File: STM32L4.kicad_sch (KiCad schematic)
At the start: 29 parts, among them J3 Conn_01x04_Pin, SW1 SW, U17 TCAN334, U18 STM32L476RGTx, U19 MR20H40, Y1 8 MHZ Oscillator

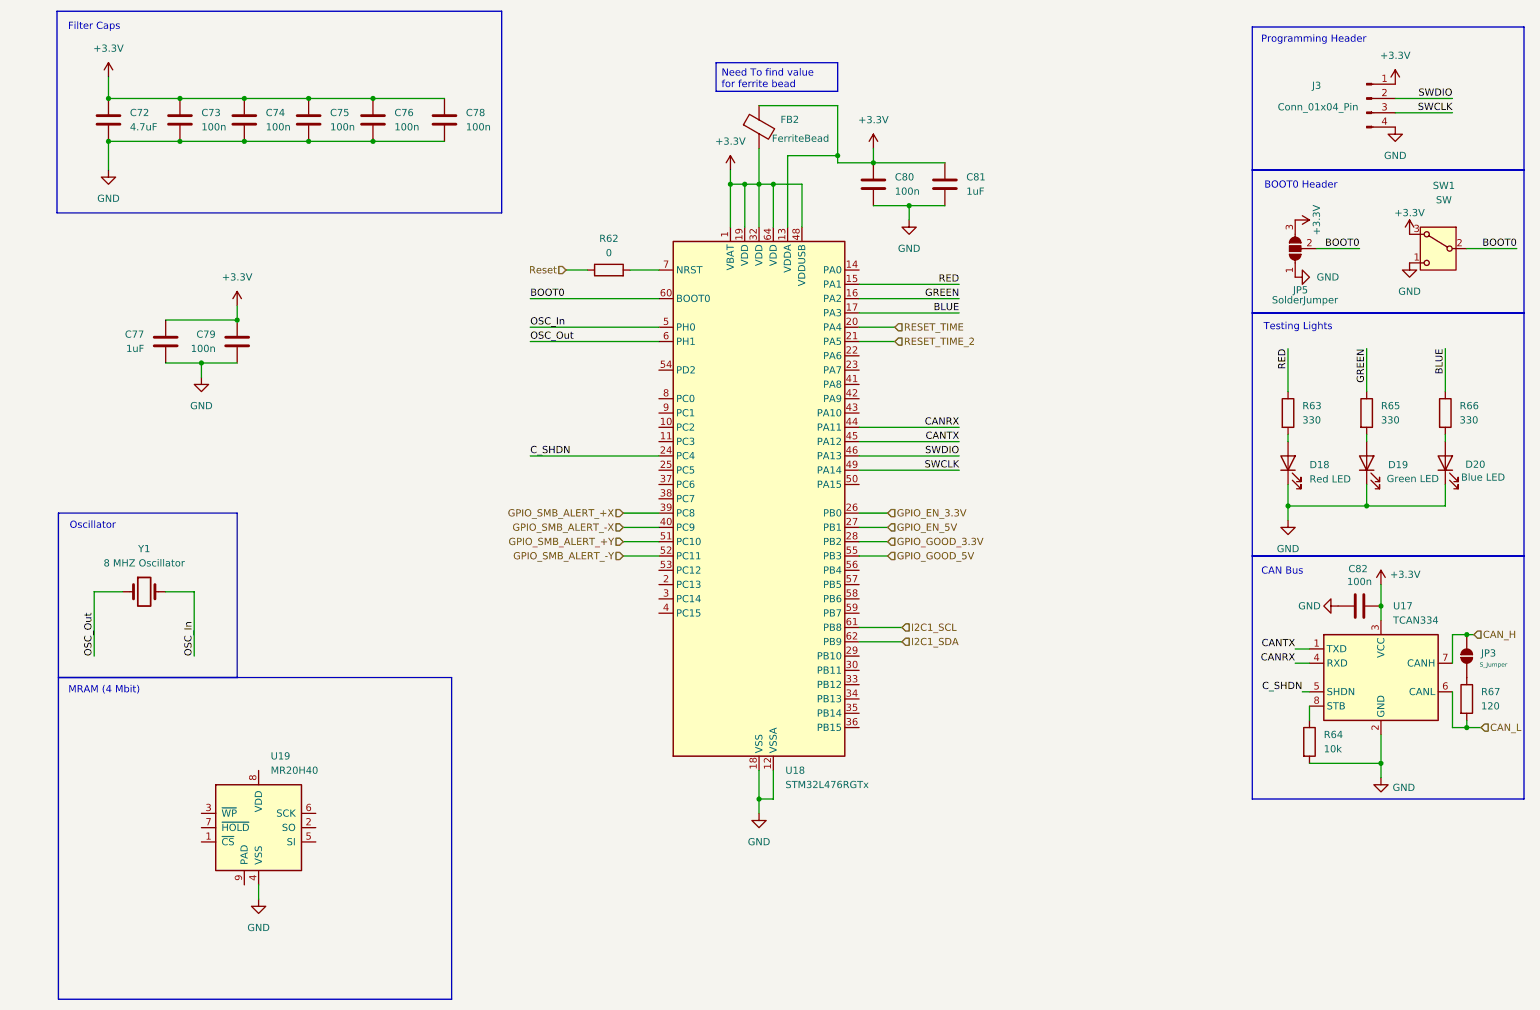
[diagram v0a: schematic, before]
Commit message: Added cap to output of lines
based on LTSpice Simulation
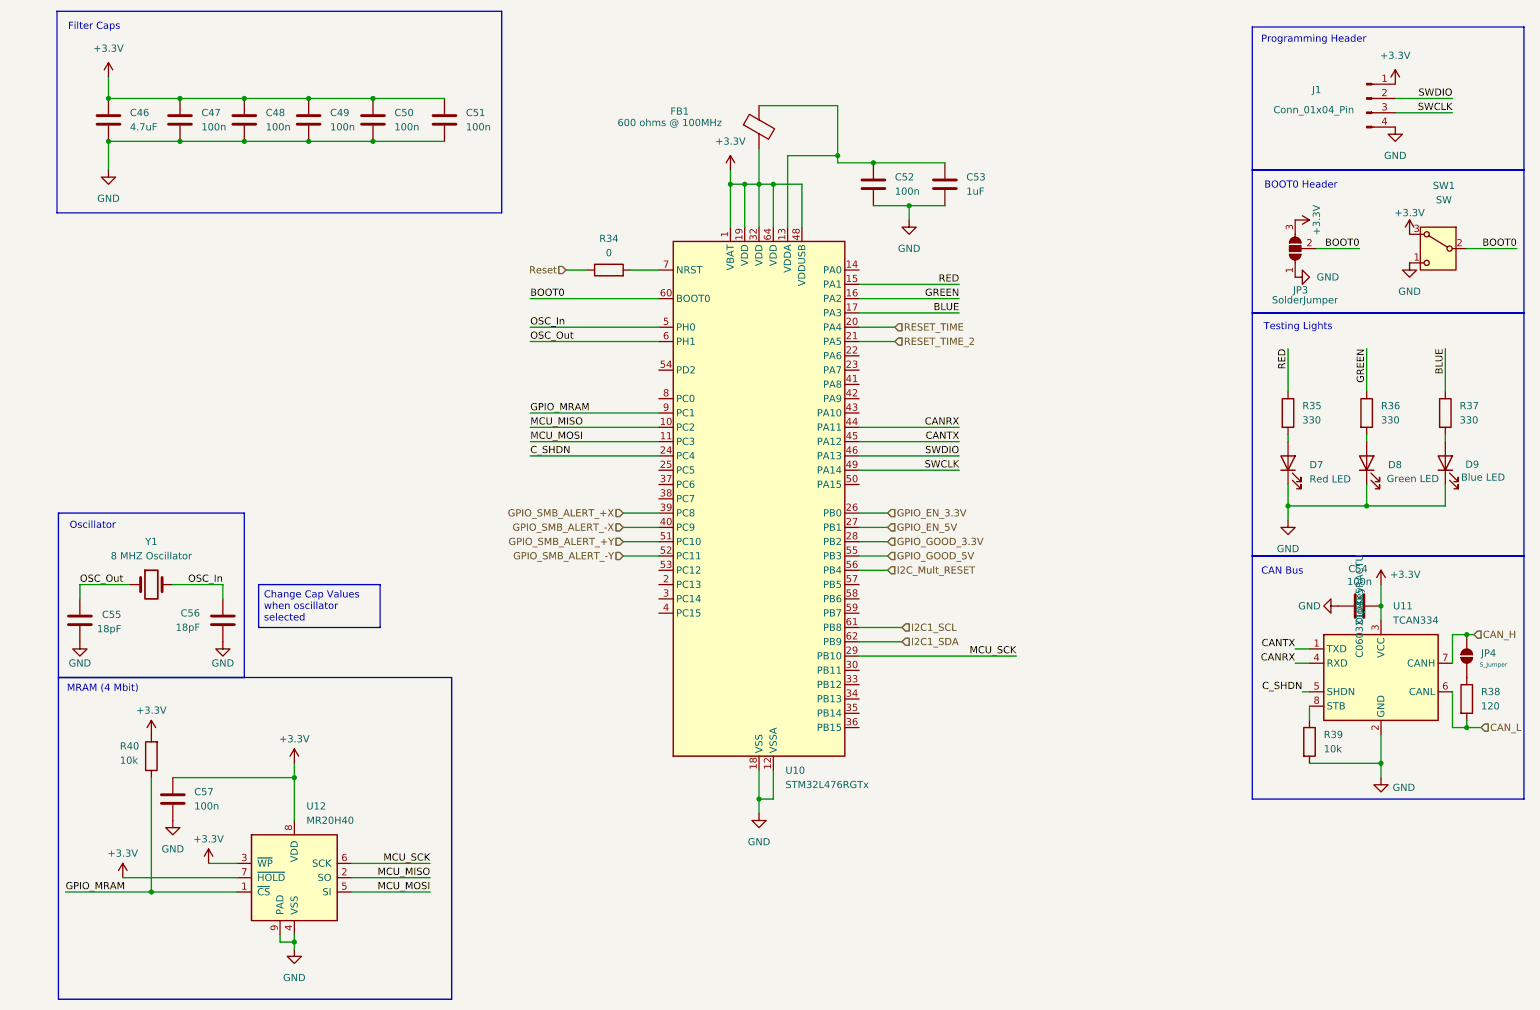
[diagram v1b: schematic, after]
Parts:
- removed C77: 1uF, symbol Device:C
- removed C79: 100n, symbol Device:C
- removed J3: Conn_01x04_Pin, symbol Connector:Conn_01x04_Pin
- added C55, C56: 18pF, symbol Device:C
- added C57: 100n, Capacitor_SMD:C_0603_1608Metric, symbol Device:C
- added J1: Conn_01x04_Pin, Connector_JST:JST_EH_B4B-EH-A_1x04_P2.50mm_Vertical, symbol Connector:Conn_01x04_Pin
- added R40: 10k, symbol Device:R
- C46: renamed from C72; footprint (none) -> Capacitor_SMD:C_0805_2012Metric
- C47: renamed from C73; footprint (none) -> Capacitor_SMD:C_0603_1608Metric; MANUFACTURER (none) -> DigiKey; MANUFACTURER_PART_NUMBER (none) -> C0603X104K5RACTU
- C48: renamed from C74; footprint (none) -> Capacitor_SMD:C_0603_1608Metric; MANUFACTURER (none) -> DigiKey; MANUFACTURER_PART_NUMBER (none) -> C0603X104K5RACTU
- C49: renamed from C75; footprint (none) -> Capacitor_SMD:C_0603_1608Metric; MANUFACTURER (none) -> DigiKey; MANUFACTURER_PART_NUMBER (none) -> C0603X104K5RACTU
- C50: renamed from C76; footprint (none) -> Capacitor_SMD:C_0603_1608Metric; MANUFACTURER (none) -> DigiKey; MANUFACTURER_PART_NUMBER (none) -> C0603X104K5RACTU
- C51: renamed from C78; footprint (none) -> Capacitor_SMD:C_0603_1608Metric; MANUFACTURER (none) -> DigiKey; MANUFACTURER_PART_NUMBER (none) -> C0603X104K5RACTU
- C52: renamed from C80; footprint (none) -> Capacitor_SMD:C_0603_1608Metric; MANUFACTURER (none) -> DigiKey; MANUFACTURER_PART_NUMBER (none) -> C0603X104K5RACTU
- C54: renamed from C82; footprint (none) -> Capacitor_SMD:C_0603_1608Metric; MANUFACTURER (none) -> DigiKey; MANUFACTURER_PART_NUMBER (none) -> C0603X104K5RACTU
- FB1: renamed from FB2; value FerriteBead -> 600 ohms @ 100MHz
- JP3: renamed from JP5; footprint (none) -> Jumper:SolderJumper-2_P1.3mm_Open_TrianglePad1.0x1.5mm
- U10: renamed from U18; footprint Package_QFP:LQFP-64_10x10mm_P0.5mm -> LTC4162IUFD-LADM_PBF:QFN50P500X400X80-29N
- U11: renamed from U17; footprint (none) -> LTC4162IUFD-LADM_PBF:QFN50P500X400X80-29N
- U12: renamed from U19; footprint (none) -> DBV5
- renumbered C81 to C53, D18 to D7, D19 to D8, D20 to D9, JP3 to JP4, R62 to R34, R63 to R35, R65 to R36, R66 to R37, R67 to R38, R64 to R39
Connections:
- net +3.3V: now also U12.3 (~{WP}), U12.7 (~{HOLD}), U12.8 (VDD), C57.2, J1.1 (Pin_1), R40.2; no longer C52.1, C53.1, FB1.1, U10.13 (VDDA)
- net GND: now also U12.9 (PAD), C55.2, C56.2, C57.1, J1.4 (Pin_4)
- net OSC_In: now also C56.1
- net OSC_Out: now also C55.1
- net SWCLK: now also J1.3 (Pin_3)
- net SWDIO: now also J1.2 (Pin_2)
- net MCU_MISO: now reaches U10.10 (PC2)
- net MCU_MISO: now also U12.2 (SO)
- net MCU_MOSI: now reaches U10.11 (PC3)
- net MCU_MOSI: now also U12.5 (SI)
- net MCU_SCK: now reaches U10.29 (PB10)
- net MCU_SCK: now also U12.6 (SCK)
- net I2C_Mult_RESET: now reaches U10.56 (PB4)
- net GPIO_MRAM: now reaches U10.9 (PC1)
- net GPIO_MRAM: now also U12.1 (~{CS}), R40.1
- new net: C52.1, C53.1, FB1.1, U10.13 (VDDA)
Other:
- company: (none) -> QSET (Jaron Cyna)
- title: (none) -> STM32L4 Schematic
- moved on the sheet: U12, Y1

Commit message: Added footprints to caps
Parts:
- C50: renamed from C53; footprint (none) -> Capacitor_SMD:C_0603_1608Metric
- C52: renamed from C55; value 18pF -> 10pF; footprint (none) -> Capacitor_SMD:C_01005_0402Metric; MANUFACTURER (none) -> DigiKey; MANUFACTURER_PART_NUMBER (none) -> GRM1555C1H100FA01D
- C53: renamed from C56; value 18pF -> 10pF; footprint (none) -> Capacitor_SMD:C_01005_0402Metric; MANUFACTURER (none) -> DigiKey; MANUFACTURER_PART_NUMBER (none) -> GRM1555C1H100FA01D
- D7, D8, D9: footprint (none) -> LED_SMD:LED_0603_1608Metric
- FB1: footprint (none) -> Inductor_SMD:L_0603_1608Metric
- R35, R36, R37: footprint (none) -> Resistor_SMD:R_0603_1608Metric
- Y1: footprint (none) -> Oscillator:Oscillator_SMD_EuroQuartz_XO32-4Pin_3.2x2.5mm
- renumbered C46 to C43, C47 to C44, C48 to C45, C49 to C46, C50 to C47, C51 to C48, C52 to C49, C54 to C51, C57 to C54
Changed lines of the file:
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@@
 		)
 	)
-	(text_box "Change Cap Values when oscillator selected"
-		(exclude_from_sim no)
-		(at 53.34 118.11 0)
-		(size 21.59 7.62)
-		(margins 0.9525 0.9525 0.9525 0.9525)
-		(stroke
-			(width 0)
-			(type solid)
-		)
-		(fill
-			(type color)
-			(color 158 218 255 1)
-		)
-		(effects
-			(font
-				(size 1.27 1.27)
-			)
-			(justify left top)
-		)
-	)
 	(junction
 		(at 62.23 31.75)
@@
 			)
 		)
-		(property "Footprint" ""
+		(property "Footprint" "Inductor_SMD:L_0603_1608Metric"
 			(at 140.462 36.83 90)
 			(effects
@@
 			)
 		)
-		(property "Footprint" ""
+		(property "Footprint" "LED_SMD:LED_0603_1608Metric"
 			(at 250.19 96.52 0)
 			(effects
@@
 		(dnp no)
 		(fields_autoplaced yes)
-		(property "Reference" "C51"
+		(property "Reference" "C48"
 			(at 90.17 34.2899 0)
 			(effects
@@
 			(project "EPS_mppt_board"
 				(path "/8f246f89-1ec7-4136-9977-839b50e116ed/bc2f1682-e3ae-4ffc-84d8-70ef19ac3f89"
-					(reference "C51")
+					(reference "C48")
 					(unit 1)
 				)
@@
 		(on_board yes)
 		(dnp no)
-		(property "Reference" "C54"
+		(property "Reference" "C51"
 			(at 248.666 115.316 90)
 			(effects
@@
 			(project "EPS_mppt_board"
 				(path "/8f246f89-1ec7-4136-9977-839b50e116ed/bc2f1682-e3ae-4ffc-84d8-70ef19ac3f89"
-					(reference "C54")
+					(reference "C51")
 					(unit 1)
 				)
@@
 		(dnp no)
 		(fields_autoplaced yes)
-		(property "Reference" "C49"
+		(property "Reference" "C46"
 			(at 66.04 34.2899 0)
 			(effects
@@
 			(project "EPS_mppt_board"
 				(path "/8f246f89-1ec7-4136-9977-839b50e116ed/bc2f1682-e3ae-4ffc-84d8-70ef19ac3f89"
-					(reference "C49")
+					(reference "C46")
 					(unit 1)
 				)
@@
 		(on_board yes)
 		(dnp no)
-		(property "Reference" "C57"
+		(property "Reference" "C54"
 			(at 41.91 154.9399 0)
 			(effects
@@
 			(project "EPS_mppt_board"
 				(path "/8f246f89-1ec7-4136-9977-839b50e116ed/bc2f1682-e3ae-4ffc-84d8-70ef19ac3f89"
-					(reference "C57")
+					(reference "C54")
 					(unit 1)
 				)
@@
 			)
 		)
-		(property "Footprint" ""
+		(property "Footprint" "Oscillator:Oscillator_SMD_EuroQuartz_XO32-4Pin_3.2x2.5mm"
 			(at 34.29 118.11 0)
 			(effects
@@
 		(dnp no)
 		(fields_autoplaced yes)
-		(property "Reference" "C47"
+		(property "Reference" "C44"
 			(at 43.18 34.2899 0)
 			(effects
@@
 			(project "EPS_mppt_board"
 				(path "/8f246f89-1ec7-4136-9977-839b50e116ed/bc2f1682-e3ae-4ffc-84d8-70ef19ac3f89"
-					(reference "C47")
+					(reference "C44")
 					(unit 1)
 				)
@@
 		(dnp no)
 		(fields_autoplaced yes)
-		(property "Reference" "C48"
+		(property "Reference" "C45"
 			(at 54.61 34.2899 0)
 			(effects
@@
 			(project "EPS_mppt_board"
 				(path "/8f246f89-1ec7-4136-9977-839b50e116ed/bc2f1682-e3ae-4ffc-84d8-70ef19ac3f89"
-					(reference "C48")
+					(reference "C45")
 					(unit 1)
 				)
@@
 		(dnp no)
 		(fields_autoplaced yes)
-		(property "Reference" "C46"
+		(property "Reference" "C43"
 			(at 30.48 34.2899 0)
 			(effects
@@
 			(project "EPS_mppt_board"
 				(path "/8f246f89-1ec7-4136-9977-839b50e116ed/bc2f1682-e3ae-4ffc-84d8-70ef19ac3f89"
-					(reference "C46")
+					(reference "C43")
 					(unit 1)
 				)
@@
 			)
 		)
-		(property "Footprint" ""
+		(property "Footprint" "Resistor_SMD:R_0603_1608Metric"
 			(at 234.442 87.63 90)
 			(effects
@@
 		(dnp no)
 		(fields_autoplaced yes)
-		(property "Reference" "C53"
+		(property "Reference" "C50"
 			(at 179.07 45.7199 0)
 			(effects
@@
 			)
 		)
-		(property "Footprint" ""
+		(property "Footprint" "Capacitor_SMD:C_0603_1608Metric"
 			(at 176.2252 50.8 0)
 			(effects
@@
 			(project "EPS_mppt_board"
 				(path "/8f246f89-1ec7-4136-9977-839b50e116ed/bc2f1682-e3ae-4ffc-84d8-70ef19ac3f89"
-					(reference "C53")
+					(reference "C50")
 					(unit 1)
 				)
@@
 			)
 		)
-		(property "Footprint" ""
+		(property "Footprint" "Resistor_SMD:R_0603_1608Metric"
 			(at 248.412 87.63 90)
 			(effects
@@
 		(dnp no)
 		(fields_autoplaced yes)
-		(property "Reference" "C50"
+		(property "Reference" "C47"
 			(at 77.47 34.2899 0)
 			(effects
@@
 			(project "EPS_mppt_board"
 				(path "/8f246f89-1ec7-4136-9977-839b50e116ed/bc2f1682-e3ae-4ffc-84d8-70ef19ac3f89"
-					(reference "C50")
+					(reference "C47")
 					(unit 1)
 				)
@@
 		(on_board yes)
 		(dnp no)
-		(property "Reference" "C56"
+		(property "Reference" "C53"
 			(at 42.926 123.19 0)
 			(effects
@@
 			)
 		)
-		(property "Value" "18pF"
+		(property "Value" "10pF"
 			(at 42.926 125.73 0)
 			(effects
@@
 			)
 		)
-		(property "Footprint" ""
+		(property "Footprint" "Capacitor_SMD:C_01005_0402Metric"
 			(at 46.0248 128.27 0)
 			(effects
@@
 			)
 		)
+		(property "MANUFACTURER" "DigiKey"
+			(at 46.99 124.46 0)
+			(effects
+				(font
+					(size 1.27 1.27)
+				)
+			)
+		)
+		(property "MANUFACTURER_PART_NUMBER" "GRM1555C1H100FA01D"
+			(at 46.99 124.46 0)
+			(effects
+				(font
+					(size 1.27 1.27)
+				)
+			)
+		)
 		(pin "2"
 		)
@@
 			(project "EPS_mppt_board"
 				(path "/8f246f89-1ec7-4136-9977-839b50e116ed/bc2f1682-e3ae-4ffc-84d8-70ef19ac3f89"
-					(reference "C56")
+					(reference "C53")
 					(unit 1)
 				)
@@
 		(dnp no)
 		(fields_autoplaced yes)
-		(property "Reference" "C52"
+		(property "Reference" "C49"
 			(at 166.37 45.7199 0)
 			(effects
@@
 			(project "EPS_mppt_board"
 				(path "/8f246f89-1ec7-4136-9977-839b50e116ed/bc2f1682-e3ae-4ffc-84d8-70ef19ac3f89"
-					(reference "C52")
+					(reference "C49")
 					(unit 1)
 				)
@@
 		(on_board yes)
 		(dnp no)
-		(property "Reference" "C55"
+		(property "Reference" "C52"
 			(at 28.956 123.444 0)
 			(effects
@@
 			)
 		)
-		(property "Value" "18pF"
+		(property "Value" "10pF"
 			(at 28.956 125.984 0)
 			(effects
@@
 			)
 		)
-		(property "Footprint" ""
+		(property "Footprint" "Capacitor_SMD:C_01005_0402Metric"
 			(at 20.6248 128.27 0)
 			(effects
@@
 			)
 		)
+		(property "MANUFACTURER" "DigiKey"
+			(at 21.59 124.46 0)
+			(effects
+				(font
+					(size 1.27 1.27)
+				)
+			)
+		)
+		(property "MANUFACTURER_PART_NUMBER" "GRM1555C1H100FA01D"
+			(at 21.59 124.46 0)
+			(effects
+				(font
+					(size 1.27 1.27)
+				)
+			)
+		)
 		(pin "2"
 		)
@@
 			(project "EPS_mppt_board"
 				(path "/8f246f89-1ec7-4136-9977-839b50e116ed/bc2f1682-e3ae-4ffc-84d8-70ef19ac3f89"
-					(reference "C55")
+					(reference "C52")
 					(unit 1)
 				)
@@
 			)
 		)
-		(property "Footprint" ""
+		(property "Footprint" "Resistor_SMD:R_0603_1608Metric"
 			(at 262.382 87.63 90)
 			(effects
@@
 			)
 		)
-		(property "Footprint" ""
+		(property "Footprint" "LED_SMD:LED_0603_1608Metric"
 			(at 236.22 96.52 0)
 			(effects
@@
 			)
 		)
-		(property "Footprint" ""
+		(property "Footprint" "LED_SMD:LED_0603_1608Metric"
 			(at 264.16 96.52 0)
 			(effects
